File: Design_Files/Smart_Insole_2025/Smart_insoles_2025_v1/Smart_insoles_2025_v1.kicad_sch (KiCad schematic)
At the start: 10 parts, among them U1 ESP32-C3_SUPERMINI_SMD, U2 CD74HC4067M96, U3 LSM6DSO32TR

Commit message: Changed Mcu to esp32c3 mini 1 n4
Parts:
- removed U1: ESP32-C3_SUPERMINI_SMD, ESP32-C3_SUPERMINI:MODULE_ESP32-C3_SUPERMINI, symbol ESP32-C3_SUPERMINI:ESP32-C3_SUPERMINI_SMD
- added C20, C21: 0.1uF, Capacitor_SMD:C_0603_1608Metric, symbol Device:C
- added J2: USB_C_Receptacle_USB2.0_16P, Connector_USB:USB_C_Receptacle_GCT_USB4105-xx-A_16P_TopMnt_Horizontal, symbol Connector:USB_C_Receptacle_USB2.0_16P
- added R22: 10k, Resistor_SMD:R_0603_1608Metric, symbol Device:R
- added R23, R24: 5.1k 1%, symbol BatteryProtectionCircuit:R_5.1k_Ohm_1%
- added SW1: RESET, Button_Switch_THT:SW_PUSH_6mm_H4.3mm, symbol Switch:SW_Push
- added SW2: BOOT, Button_Switch_THT:SW_PUSH_6mm_H4.3mm, symbol Switch:SW_Push
- added U6: ESP32-C3-MINI-1-N4, ESP32-C3-MINI-1-N4:XCVR_ESP32-C3-MINI-1-N4, symbol ESP32-C3-MINI-1-N4:ESP32-C3-MINI-1-N4
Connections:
- net GND: now also C20.1, C21.1, J2.A1 (GND), J2.A12 (GND), J2.B1 (GND), J2.B12 (GND), J2.S1 (SHIELD), R23.2, R24.2, SW1.1, SW2.1, U6.1 (GND), U6.11 (GND__2), U6.14 (GND__3), U6.2 (GND__1), U6.36 (GND__4), U6.37 (GND__5), U6.38 (GND__6), U6.39 (GND__7), U6.40 (GND__8), U6.41 (GND__9), U6.42 (GND__10), U6.43 (GND__11), U6.44 (GND__12), U6.45 (GND__13), U6.46 (GND__14), U6.47 (GND__15), U6.48 (GND__16), U6.49_1 (GND__17), U6.49_2 (GND__18), U6.49_3 (GND__19), U6.49_4 (GND__20), U6.49_5 (GND__21), U6.49_6 (GND__22), U6.49_7 (GND__23), U6.49_8 (GND__24), U6.49_9 (GND__25), U6.50 (GND__26), U6.51 (GND__27), U6.52 (GND__28), U6.53 (GND__29)
- net INT: now also U6.19 (IO5)
- net S0: now also U6.12 (IO0)
- net S1: now also U6.13 (IO1)
- net S2: now also U6.5 (IO2)
- net S3: now also U6.6 (IO3)
- net SCL: now also U6.21 (IO7)
- net SDA: now also U6.20 (IO6)
- net SIG: now also U6.18 (IO4)
- net VCC: now also U6.3 (3V3)
- new net: C21.2, R22.2, SW1.2, U6.8 (EN)
- new net: J2.B5 (CC2), R23.1
- new net: J2.A5 (CC1), R24.1
- new net: C20.2, SW2.2
- new net +3V3: R22.1
- new net USB_N: J2.A7 (D-), J2.B7 (D-), U6.26 (IO18)
- new net USB_P: J2.A6 (D+), J2.B6 (D+), U6.27 (IO19)
- new net VBUS: J2.A4 (VBUS), J2.A9 (VBUS), J2.B4 (VBUS), J2.B9 (VBUS)
- no-connect marks 17 -> 13
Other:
- note added: "USB-C Programming Only"
- moved on the sheet: C1, C14, C15, C2, C3, R1, RN1, U2, U3

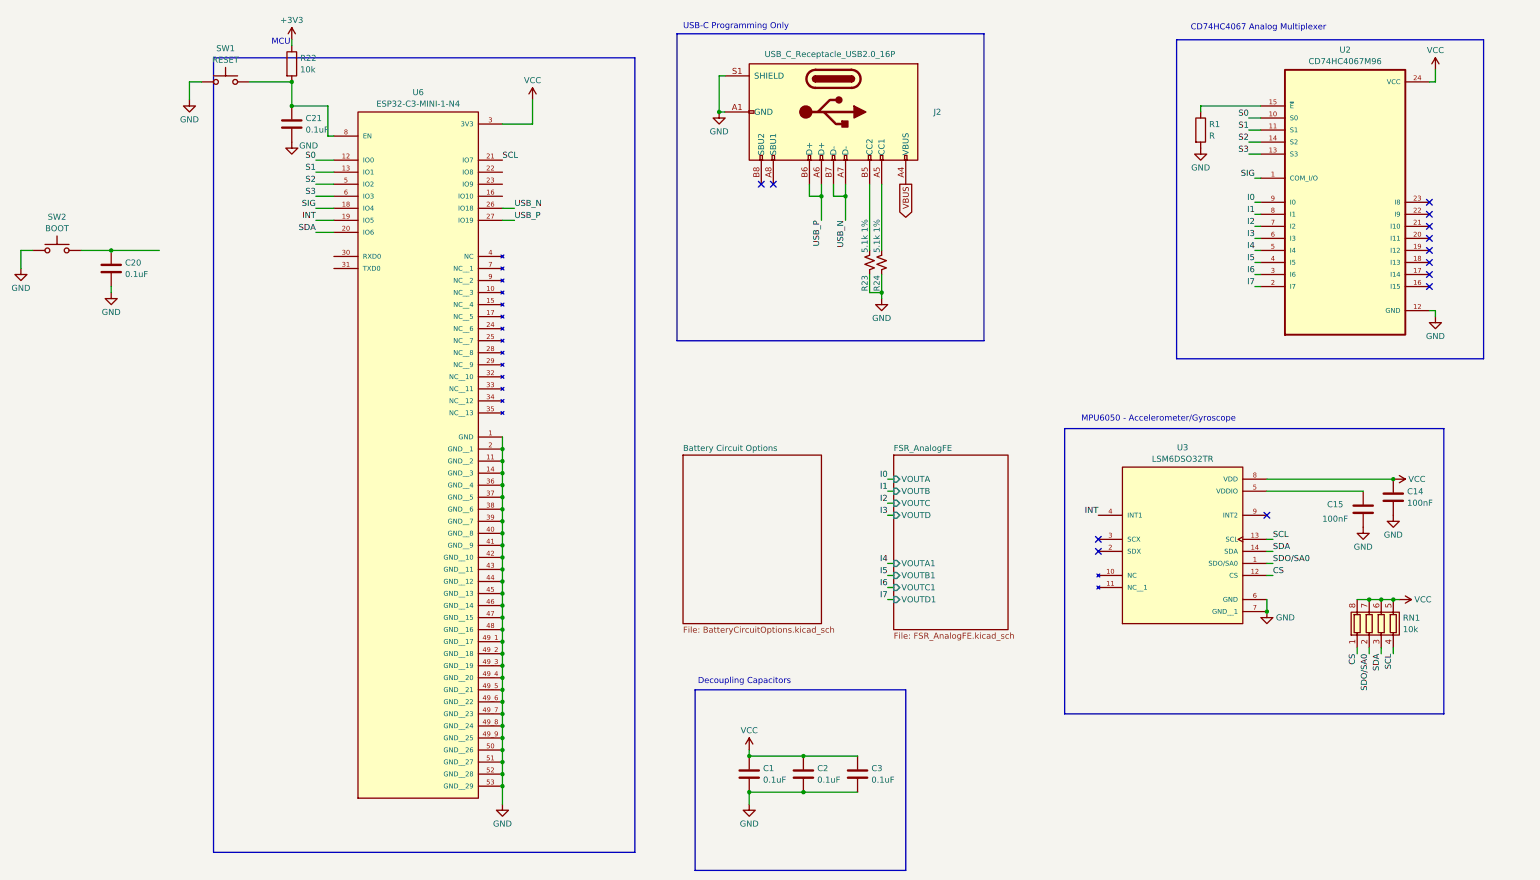
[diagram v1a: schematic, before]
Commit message: SCH: Advances in Battery circuit. Added External_Periph sheet
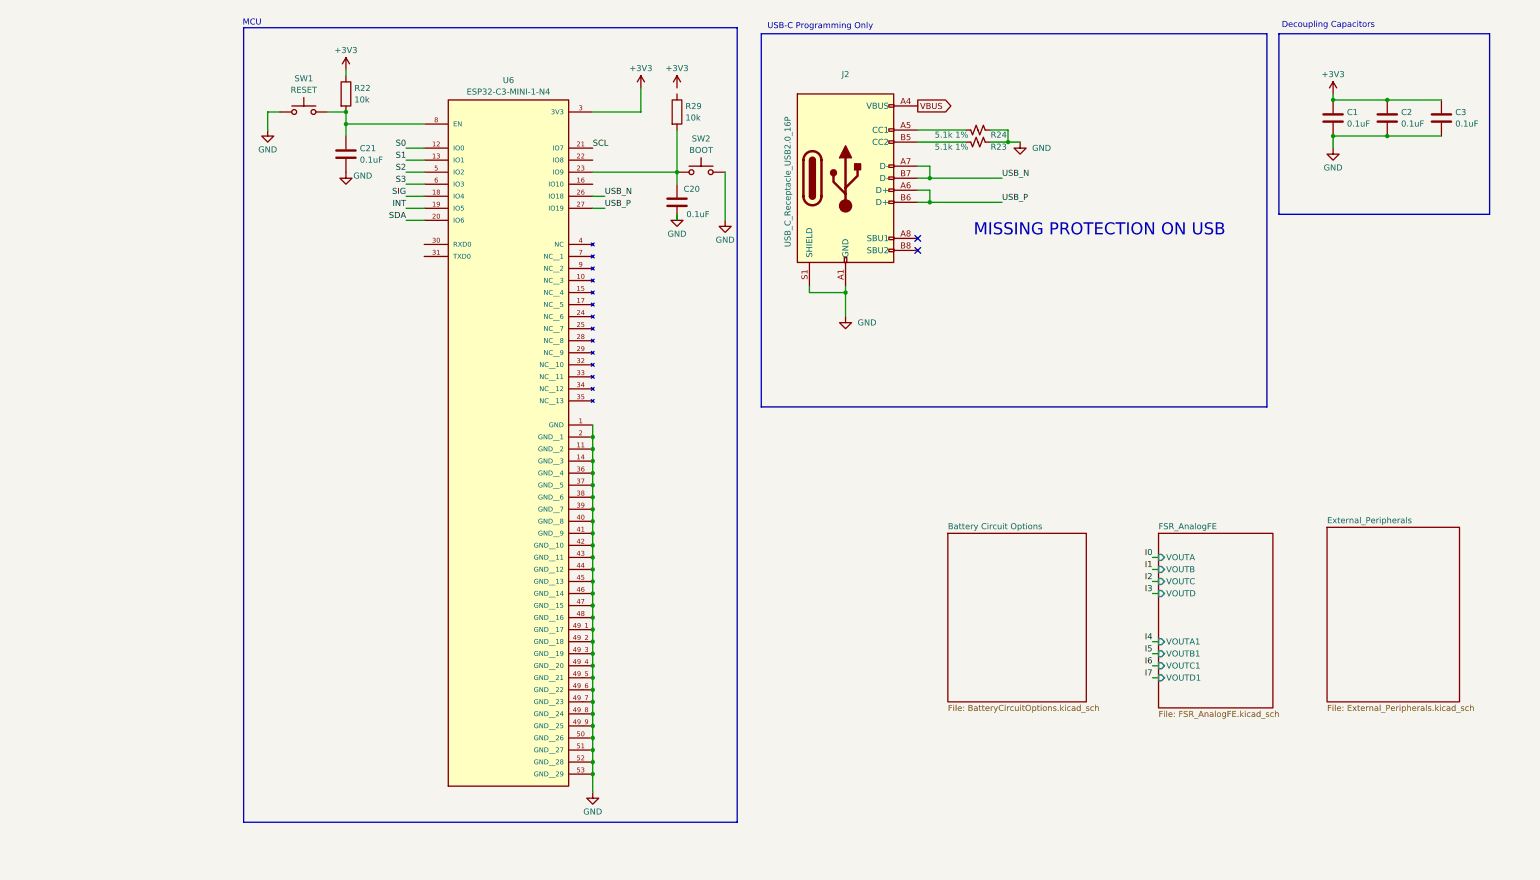
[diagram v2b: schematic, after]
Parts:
- removed C14, C15: 100nF, Capacitor_SMD:C_0603_1608Metric_Pad1.08x0.95mm_HandSolder, symbol Device:C
- removed R1: R, Resistor_SMD:R_0603_1608Metric_Pad0.98x0.95mm_HandSolder, symbol Device:R
- removed RN1: 10k, Resistor_SMD:R_Array_Concave_4x0603, symbol Device:R_Pack04
- removed U2: CD74HC4067M96, CD74HC4067:SOIC127P1030X265-24N, symbol CD74HC4067:CD74HC4067M96
- removed U3: LSM6DSO32TR, LDM6S032TR:XDCR_LSM6DSO32TR, symbol LSM6DSO32TR:LSM6DSO32TR
- added R29: 10k, Resistor_SMD:R_0603_1608Metric, symbol Device:R
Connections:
- net VCC is gone; now on net +3V3: C1.1, C2.1, C3.1, U6.3 (3V3)
- net at U6.23 (IO9): now also C20.2, SW2.2, R29.2
- no-connect marks 13 -> 2
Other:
- added sheet External_Peripherals (External_Peripherals.kicad_sch)
- note added: "MISSING PROTECTION ON USB"
- note removed: "CD74HC4067 Analog Multiplexer"
- note removed: "MPU6050 - Accelerometer/Gyroscope"
- moved on the sheet: C1, C2, C20, C21, C3, J2, R22, R23, R24, SW1, SW2, U6

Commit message: SCH: Added TVS diode on USB. Defined transistor and diode for battery/usb charging/switching
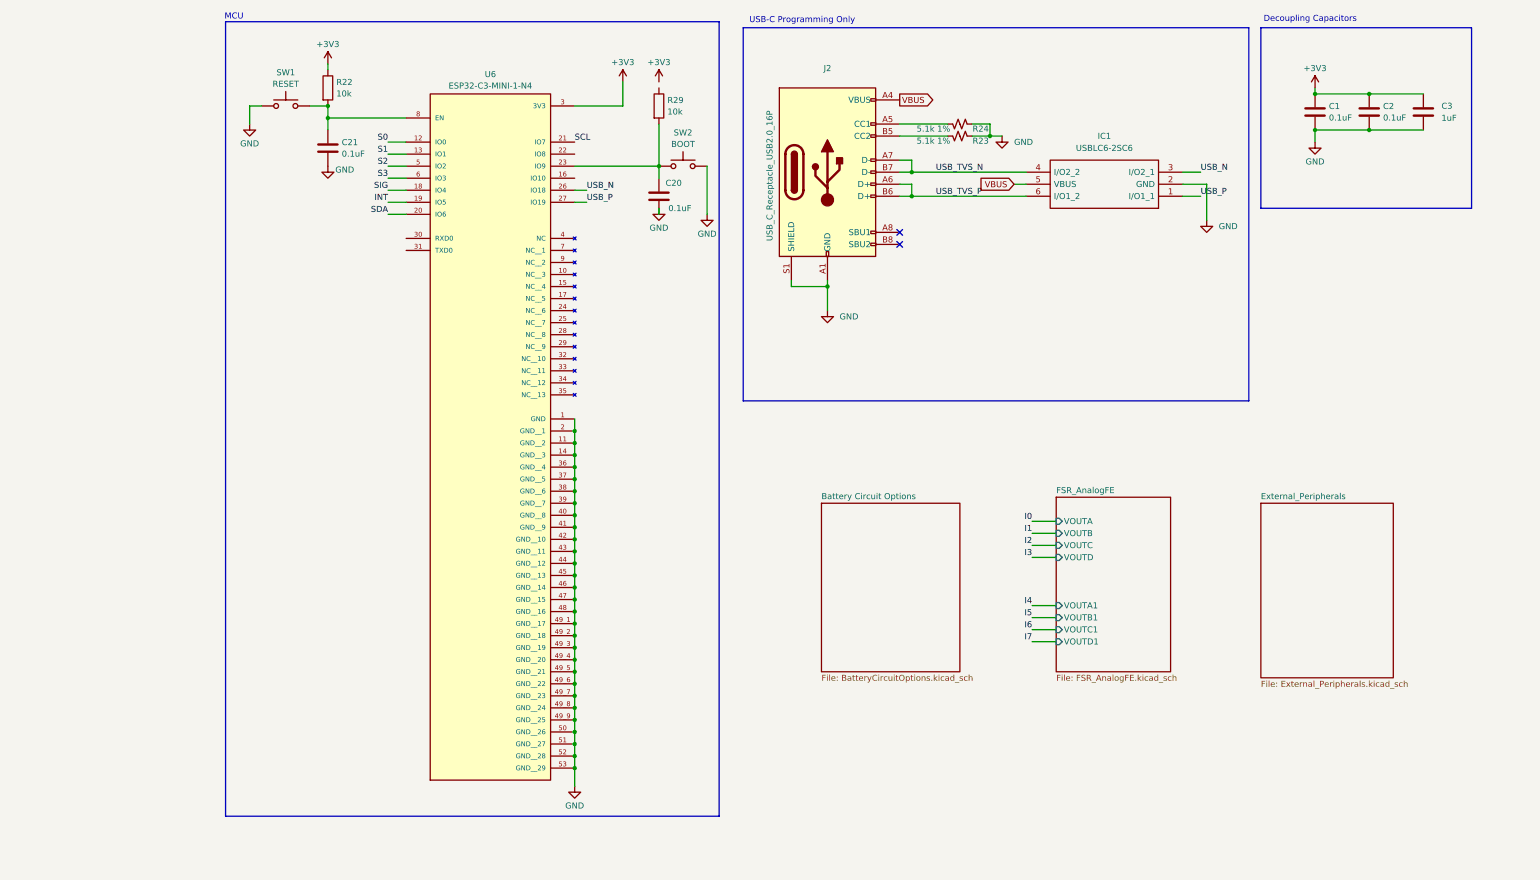
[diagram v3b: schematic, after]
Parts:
- added IC1: USBLC6-2SC6, SOT95P280X145-6N, symbol USBLC6-2SC6:USBLC6-2SC6
- C3: value 0.1uF -> 1uF
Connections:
- net GND: now also IC1.2 (GND)
- net USB_N: now also IC1.3 (I/O2_1); no longer J2.A7 (D-), J2.B7 (D-)
- net USB_P: now also IC1.1 (I/O1_1); no longer J2.A6 (D+), J2.B6 (D+)
- net VBUS: now also IC1.5 (VBUS)
- new net USB_TVS_N: IC1.4 (I/O2_2), J2.A7 (D-), J2.B7 (D-)
- new net USB_TVS_P: IC1.6 (I/O1_2), J2.A6 (D+), J2.B6 (D+)
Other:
- note removed: "MISSING PROTECTION ON USB"
- moved on the sheet: C1, C2, C20, C21, C3, J2, R22, R23, R24, R29, SW1, SW2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

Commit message: SCH:Solved Errors in ERC
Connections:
- net +3V3: now also R29.1
- no-connect marks 2 -> 6
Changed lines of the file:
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@@
 	(rectangle
 		(start 125.73 17.78)
-		(end 232.41 96.52)
+		(end 232.41 86.36)
 		(stroke
 			(width 0)
@@
 	)
 	(no_connect
+		(at 90.17 49.53)
+	)
+	(no_connect
 		(at 158.75 60.96)
 	)
+	(no_connect
+		(at 54.61 62.23)
+	)
+	(no_connect
+		(at 90.17 44.45)
+	)
+	(no_connect
+		(at 54.61 64.77)
+	)
 	(wire
 		(pts
@@
 	(wire
 		(pts
+			(xy 107.95 29.21) (xy 107.95 30.48)
+		)
+		(stroke
+			(width 0)
+			(type default)
+		)
+	)
+	(wire
+		(pts
 			(xy 246.38 41.91) (xy 246.38 39.37)
 		)
@@
 		)
 	)
-	(label "SDA"
-		(at 50.8 57.15 180)
-		(effects
-			(font
-				(size 1.27 1.27)
-			)
-			(justify right bottom)
-		)
-	)
 	(label "I1"
 		(at 186.69 124.46 180)
@@
 		)
 	)
-	(label "S1"
-		(at 50.8 44.45 180)
-		(effects
-			(font
-				(size 1.27 1.27)
-			)
-			(justify right bottom)
-		)
-	)
 	(label "I5"
 		(at 186.69 142.24 180)
@@
 		)
 	)
-	(label "S3"
-		(at 50.8 49.53 180)
+	(label "I6"
+		(at 186.69 144.78 180)
 		(effects
 			(font
@@
 		)
 	)
-	(label "S2"
-		(at 50.8 46.99 180)
+	(label "I0"
+		(at 186.69 121.92 180)
 		(effects
 			(font
@@
 		)
 	)
-	(label "I6"
-		(at 186.69 144.78 180)
+	(label "I7"
+		(at 186.69 147.32 180)
 		(effects
 			(font
@@
 		)
 	)
-	(label "I0"
-		(at 186.69 121.92 180)
+	(label "I4"
+		(at 186.69 139.7 180)
 		(effects
 			(font
@@
 		)
 	)
-	(label "I7"
-		(at 186.69 147.32 180)
+	(label "USB_P"
+		(at 92.71 54.61 0)
 		(effects
 			(font
 				(size 1.27 1.27)
 			)
-			(justify right bottom)
+			(justify left bottom)
 		)
 	)
-	(label "I4"
-		(at 186.69 139.7 180)
+	(label "I2"
+		(at 186.69 127 180)
 		(effects
 			(font
@@
 		)
 	)
-	(label "S0"
-		(at 50.8 41.91 180)
+	(label "USB_N"
+		(at 222.25 48.26 0)
 		(effects
 			(font
 				(size 1.27 1.27)
 			)
-			(justify right bottom)
+			(justify left bottom)
 		)
 	)
-	(label "SCL"
-		(at 90.17 41.91 0)
+	(label "I3"
+		(at 186.69 129.54 180)
 		(effects
 			(font
 				(size 1.27 1.27)
 			)
-			(justify left bottom)
+			(justify right bottom)
 		)
 	)
-	(label "USB_P"
-		(at 92.71 54.61 0)
+	(global_label "VBUS"
+		(shape input)
+		(at 182.88 50.8 180)
 		(effects
 			(font
 				(size 1.27 1.27)
 			)
-			(justify left bottom)
+			(justify right)
+		)
+		(property "Intersheetrefs" "${INTERSHEET_REFS}"
+			(at 182.88 50.8 90)
+			(effects
+				(font
+					(size 1.27 1.27)
+				)
+				(hide yes)
+			)
 		)
 	)
-	(label "SIG"
-		(at 50.8 52.07 180)
+	(global_label "INT"
+		(shape input)
+		(at 50.8 54.61 180)
+		(fields_autoplaced yes)
 		(effects
 			(font
 				(size 1.27 1.27)
 			)
-			(justify right bottom)
+			(justify right)
+		)
+		(property "Intersheetrefs" "${INTERSHEET_REFS}"
+			(at 44.9119 54.61 0)
+			(effects
+				(font
+					(size 1.27 1.27)
+				)
+				(justify right)
+				(hide yes)
+			)
 		)
 	)
-	(label "I2"
-		(at 186.69 127 180)
+	(global_label "S1"
+		(shape input)
+		(at 50.8 44.45 180)
+		(fields_autoplaced yes)
 		(effects
 			(font
 				(size 1.27 1.27)
 			)
-			(justify right bottom)
+			(justify right)
+		)
+		(property "Intersheetrefs" "${INTERSHEET_REFS}"
+			(at 45.3958 44.45 0)
+			(effects
+				(font
+					(size 1.27 1.27)
+				)
+				(justify right)
+				(hide yes)
+			)
 		)
 	)
-	(label "INT"
-		(at 50.8 54.61 180)
+	(global_label "S2"
+		(shape input)
+		(at 50.8 46.99 180)
+		(fields_autoplaced yes)
 		(effects
 			(font
 				(size 1.27 1.27)
 			)
-			(justify right bottom)
+			(justify right)
+		)
+		(property "Intersheetrefs" "${INTERSHEET_REFS}"
+			(at 45.3958 46.99 0)
+			(effects
+				(font
+					(size 1.27 1.27)
+				)
+				(justify right)
+				(hide yes)
+			)
 		)
 	)
-	(label "USB_N"
-		(at 222.25 48.26 0)
+	(global_label "S0"
+		(shape input)
+		(at 50.8 41.91 180)
+		(fields_autoplaced yes)
 		(effects
 			(font
 				(size 1.27 1.27)
 			)
-			(justify left bottom)
+			(justify right)
+		)
+		(property "Intersheetrefs" "${INTERSHEET_REFS}"
+			(at 45.3958 41.91 0)
+			(effects
+				(font
+					(size 1.27 1.27)
+				)
+				(justify right)
+				(hide yes)
+			)
 		)
 	)
-	(label "I3"
-		(at 186.69 129.54 180)
+	(global_label "SDA"
+		(shape input)
+		(at 50.8 57.15 180)
+		(fields_autoplaced yes)
 		(effects
 			(font
 				(size 1.27 1.27)
 			)
-			(justify right bottom)
+			(justify right)
+		)
+		(property "Intersheetrefs" "${INTERSHEET_REFS}"
+			(at 44.2467 57.15 0)
+			(effects
+				(font
+					(size 1.27 1.27)
+				)
+				(justify right)
+				(hide yes)
+			)
 		)
 	)
-	(global_label "VBUS"
+	(global_label "SIG"
 		(shape input)
-		(at 182.88 50.8 180)
+		(at 50.8 52.07 180)
+		(fields_autoplaced yes)
 		(effects
 			(font
@@
 		)
 		(property "Intersheetrefs" "${INTERSHEET_REFS}"
-			(at 182.88 50.8 90)
+			(at 44.7305 52.07 0)
 			(effects
 				(font
 					(size 1.27 1.27)
 				)
+				(justify right)
 				(hide yes)
 			)
@@
 		)
 	)
+	(global_label "S3"
+		(shape input)
+		(at 50.8 49.53 180)
+		(fields_autoplaced yes)
+		(effects
+			(font
+				(size 1.27 1.27)
+			)
+			(justify right)
+		)
+		(property "Intersheetrefs" "${INTERSHEET_REFS}"
+			(at 45.3958 49.53 0)
+			(effects
+				(font
+					(size 1.27 1.27)
+				)
+				(justify right)
+				(hide yes)
+			)
+		)
+	)
+	(global_label "SCL"
+		(shape output)
+		(at 90.17 41.91 0)
+		(fields_autoplaced yes)
+		(effects
+			(font
+				(size 1.27 1.27)
+			)
+			(justify left)
+		)
+		(property "Intersheetrefs" "${INTERSHEET_REFS}"
+			(at 96.6628 41.91 0)
+			(effects
+				(font
+					(size 1.27 1.27)
+				)
+				(justify left)
+				(hide yes)
+			)
+		)
+	)
 	(symbol
 		(lib_id "USBLC6-2SC6:USBLC6-2SC6")
@@
 		(lib_id "power:+3V3")
 		(at 107.95 29.21 0)
+		(mirror y)
 		(unit 1)
 		(exclude_from_sim no)
@@
 		(on_board yes)
 		(dnp no)
-		(fields_autoplaced yes)
 		(property "Reference" "#PWR059"
 			(at 107.95 33.02 0)

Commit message: SCH: Added missing footprints. PCB: Grouped related components for new layout
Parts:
- C1, C2, C3: footprint Capacitor_SMD:C_0603_1608Metric_Pad1.08x0.95mm_HandSolder -> Capacitor_SMD:C_0805_2012Metric_Pad1.18x1.45mm_HandSolder
- C20, C21: footprint Capacitor_SMD:C_0603_1608Metric -> Capacitor_SMD:C_0805_2012Metric_Pad1.18x1.45mm_HandSolder
- IC1: footprint SOT95P280X145-6N -> USBLC6-2SC6:SOT95P280X145-6N
- R23, R24: footprint (none) -> Capacitor_SMD:C_0805_2012Metric_Pad1.18x1.45mm_HandSolder
- SW1, SW2: footprint Button_Switch_THT:SW_PUSH_6mm_H4.3mm -> Button_Switch_SMD:SW_Push_SPST_NO_Alps_SKRK
